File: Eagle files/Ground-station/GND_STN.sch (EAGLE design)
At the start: 43 parts, among them IC1 BMP280, J2 XT60-M, Q3 SI7625DN-T1-GE3, U1 AMS1117-5.0, U2 AMS1117-3.3, U4 SOIC127P790X216-8NW25Q128JVJSQ, X1 USB Type C

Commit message: Added the GND_STN.brd file
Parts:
- removed C10, C11, C12, C15, C16, C4, C5, C8, C9: 100nF, rcl:C-EUC0603
- added R10, R8: 10k, rcl:R-EU_R0603
- added R3, R6: 27.4, rcl:R-EU_R0603
- C13, C18, C2, C3: device rcl:C-EUC0805 -> rcl:C-EUC0603
- C6, C7: value 1uF -> 10uF
- R19, R22, R23, R9: device rcl:R-EU_R0805 -> rcl:R-EU_R0603
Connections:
- removed net 3V3_OP: C10.1, C11.1, C12.1, C15.1, C16.1, C7.1, C8.1, C9.1, RP2040.ADC_AVDD, RP2040.IOVDD0, RP2040.IOVDD1, RP2040.IOVDD2, RP2040.IOVDD3, RP2040.IOVDD4, RP2040.IOVDD5, RP2040.RUN, RP2040.USB_VDD, RP2040.VREG_IN, U4.VCC
- removed net N$3: C2.1
- new net N$4: R3.1, RP2040.USB_DP
- new net N$5: R6.1, RP2040.USB_DM
- new net N$6: C24.2, R1.1, U$3.TRI
- net 1V1: no longer C4.1, C5.1
- net 3V3: now also C7.1, R10.1, R8.2, RP2040.ADC_AVDD, RP2040.IOVDD0, RP2040.IOVDD1, RP2040.IOVDD2, RP2040.IOVDD3, RP2040.IOVDD4, RP2040.IOVDD5, RP2040.RUN, RP2040.USB_VDD, RP2040.VREG_IN, U4.VCC
- net 5V: now also C2.1
- net 5V_BATT: now also D4.A; no longer D4.C, Q3.S_1, Q3.S_2, Q3.S_3
- net D+: now also R3.2
- net D-: now also R6.2
- net GND: no longer C10.2, C11.2, C12.2, C15.2, C16.2, C4.2, C5.2, C8.2, C9.2
- net N$1: now also D4.C, Q3.S_1, Q3.S_2, Q3.S_3; no longer D4.A
- net RSSI: now also RP2040.GPIO23
- net SCK: no longer RP2040.GPIO10
- net TEL_RST: now also RP2040.GPIO22
- net TEL_RX: now also R8.1, RP2040.GPIO24
- net TEL_TX: now also R10.2, RP2040.GPIO25
- net XOUT: no longer C24.2, R1.1, U$3.TRI
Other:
- moved on the sheet: C6

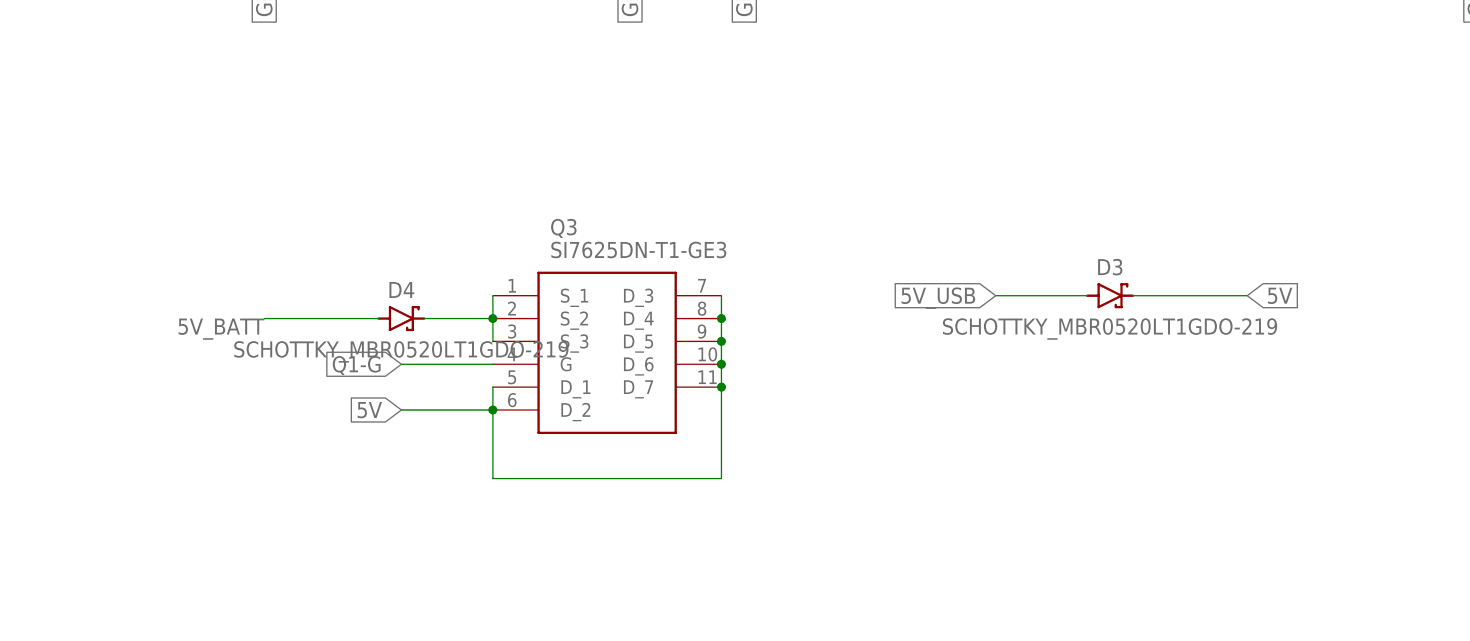
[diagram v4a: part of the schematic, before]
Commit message: Updated the traces
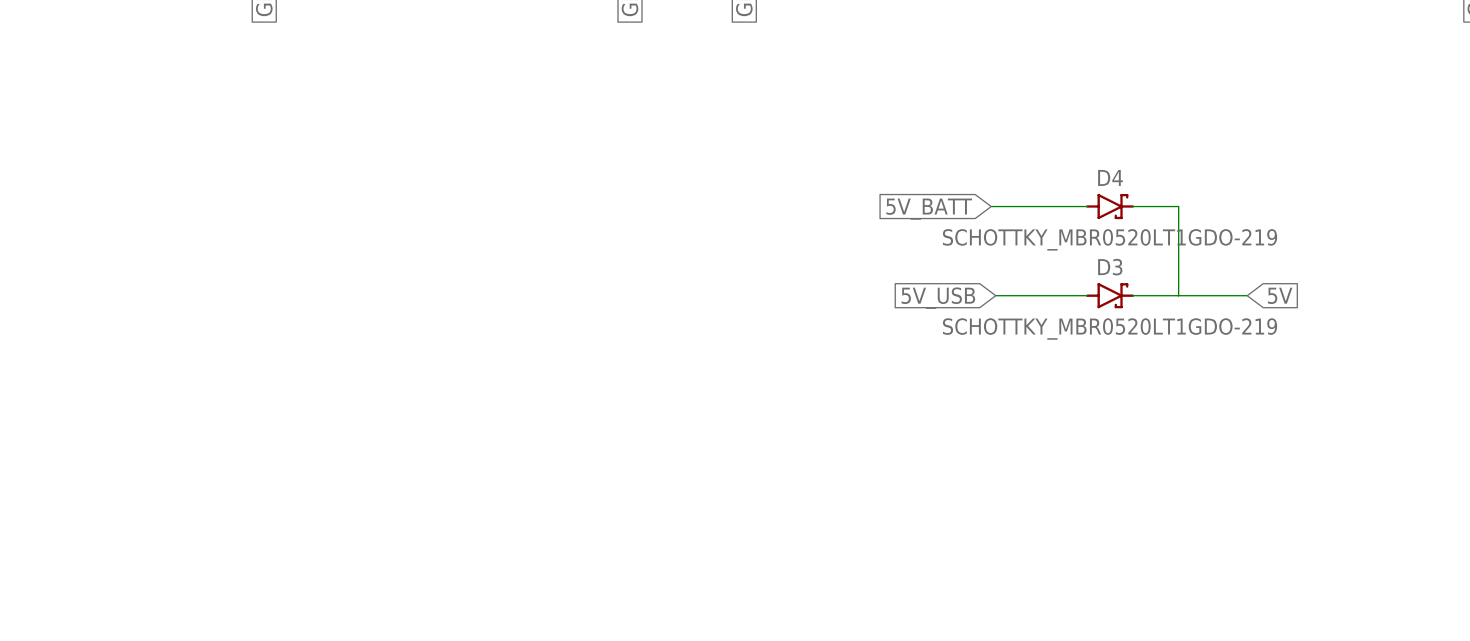
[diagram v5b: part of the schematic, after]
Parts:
- removed Q3: SI7625DN-T1-GE3, SI7625DN-T1-GE3:SI7625DN-T1-GE3
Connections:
- removed net N$1: D4.C, Q3.S_1, Q3.S_2, Q3.S_3
- removed net Q1-G: Q3.G
- net 5V: now also D4.C; no longer Q3.D_1, Q3.D_2, Q3.D_3, Q3.D_4, Q3.D_5, Q3.D_6, Q3.D_7
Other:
- moved on the sheet: D4
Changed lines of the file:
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@@
 <part name="X1" library="microbuilder" deviceset="USB_C" device="" value="USB Type C"/>
 <part name="SV1" library="con-lsta" library_urn="urn:adsk.eagle:library:161" deviceset="FE10-1" device="" package3d_urn="urn:adsk.eagle:package:8192/1"/>
-<part name="Q3" library="SI7625DN-T1-GE3" deviceset="SI7625DN-T1-GE3" device=""/>
 <part name="D3" library="Diode" library_urn="urn:adsk.eagle:library:16378169" deviceset="SCHOTTKY_" device="DO-219" package3d_urn="urn:adsk.eagle:package:9427153/2" technology="MBR0520LT1G"/>
 <part name="D4" library="Diode" library_urn="urn:adsk.eagle:library:16378169" deviceset="SCHOTTKY_" device="DO-219" package3d_urn="urn:adsk.eagle:package:9427153/2" technology="MBR0520LT1G"/>
@@
 <attribute name="NAME" x="-64.77" y="121.158" size="1.778" layer="95" rot="R180"/>
 </instance>
-<instance part="Q3" gate="G$1" x="-513.08" y="88.9" smashed="yes">
-<attribute name="NAME" x="-506.73" y="96.52" size="1.778" layer="95" align="center-left"/>
-<attribute name="VALUE" x="-506.73" y="93.98" size="1.778" layer="96" align="center-left"/>
-</instance>
 <instance part="D3" gate="G$1" x="-444.5" y="88.9" smashed="yes">
 <attribute name="NAME" x="-444.5" y="92.075" size="1.778" layer="95" align="center"/>
 <attribute name="VALUE" x="-444.5" y="85.471" size="1.778" layer="95" align="center"/>
 </instance>
-<instance part="D4" gate="G$1" x="-523.24" y="86.36" smashed="yes">
-<attribute name="NAME" x="-523.24" y="89.535" size="1.778" layer="95" align="center"/>
-<attribute name="VALUE" x="-523.24" y="82.931" size="1.778" layer="95" align="center"/>
+<instance part="D4" gate="G$1" x="-444.5" y="98.806" smashed="yes">
+<attribute name="NAME" x="-444.5" y="101.981" size="1.778" layer="95" align="center"/>
+<attribute name="VALUE" x="-444.5" y="95.377" size="1.778" layer="95" align="center"/>
 </instance>
 <instance part="U2" gate="G$1" x="-386.08" y="139.7" smashed="yes">
@@
 <segment>
 <pinref part="D3" gate="G$1" pin="C"/>
-<wire x1="-441.96" y1="88.9" x2="-429.26" y2="88.9" width="0.1524" layer="91"/>
+<wire x1="-441.96" y1="88.9" x2="-436.88" y2="88.9" width="0.1524" layer="91"/>
 <label x="-429.26" y="88.9" size="1.778" layer="95" xref="yes"/>
-</segment>
-<segment>
-<pinref part="Q3" gate="G$1" pin="D_3"/>
-<pinref part="Q3" gate="G$1" pin="D_4"/>
-<wire x1="-487.68" y1="88.9" x2="-487.68" y2="86.36" width="0.1524" layer="91"/>
-<pinref part="Q3" gate="G$1" pin="D_5"/>
-<wire x1="-487.68" y1="83.82" x2="-487.68" y2="86.36" width="0.1524" layer="91"/>
-<junction x="-487.68" y="86.36"/>
-<pinref part="Q3" gate="G$1" pin="D_6"/>
-<wire x1="-487.68" y1="83.82" x2="-487.68" y2="81.28" width="0.1524" layer="91"/>
-<junction x="-487.68" y="83.82"/>
-<pinref part="Q3" gate="G$1" pin="D_7"/>
-<wire x1="-487.68" y1="81.28" x2="-487.68" y2="78.74" width="0.1524" layer="91"/>
-<junction x="-487.68" y="81.28"/>
-<wire x1="-487.68" y1="78.74" x2="-487.68" y2="68.58" width="0.1524" layer="91"/>
-<junction x="-487.68" y="78.74"/>
-<pinref part="Q3" gate="G$1" pin="D_1"/>
-<pinref part="Q3" gate="G$1" pin="D_2"/>
-<wire x1="-487.68" y1="68.58" x2="-513.08" y2="68.58" width="0.1524" layer="91"/>
-<wire x1="-513.08" y1="78.74" x2="-513.08" y2="76.2" width="0.1524" layer="91"/>
-<wire x1="-513.08" y1="68.58" x2="-513.08" y2="76.2" width="0.1524" layer="91"/>
-<junction x="-513.08" y="76.2"/>
-<wire x1="-513.08" y1="76.2" x2="-523.24" y2="76.2" width="0.1524" layer="91"/>
-<label x="-523.24" y="76.2" size="1.778" layer="95" rot="R180" xref="yes"/>
+<wire x1="-436.88" y1="88.9" x2="-429.26" y2="88.9" width="0.1524" layer="91"/>
+<wire x1="-436.88" y1="88.9" x2="-436.88" y2="98.806" width="0.1524" layer="91"/>
+<pinref part="D4" gate="G$1" pin="C"/>
+<wire x1="-436.88" y1="98.806" x2="-441.96" y2="98.806" width="0.1524" layer="91"/>
 </segment>
 <segment>
@@
 <segment>
 <pinref part="D4" gate="G$1" pin="A"/>
-<wire x1="-525.78" y1="86.36" x2="-538.48" y2="86.36" width="0.1524" layer="91"/>
-<label x="-538.48" y="86.36" size="1.778" layer="95" rot="R180"/>
+<wire x1="-447.04" y1="98.806" x2="-457.708" y2="98.806" width="0.1524" layer="91"/>
+<label x="-457.708" y="98.806" size="1.778" layer="95" rot="R180" xref="yes"/>
 </segment>
 </net>
@@
 </segment>
 </net>
-<net name="Q1-G" class="0">
-<segment>
-<pinref part="Q3" gate="G$1" pin="G"/>
-<wire x1="-513.08" y1="81.28" x2="-523.24" y2="81.28" width="0.1524" layer="91"/>
-<label x="-523.24" y="81.28" size="1.778" layer="95" rot="R180" xref="yes"/>
-</segment>
-</net>
 <net name="SCK" class="0">
 <segment>
@@
 </segment>
 </net>
-<net name="N$1" class="0">
-<segment>
-<pinref part="D4" gate="G$1" pin="C"/>
-<pinref part="Q3" gate="G$1" pin="S_2"/>
-<wire x1="-520.7" y1="86.36" x2="-513.08" y2="86.36" width="0.1524" layer="91"/>
-<pinref part="Q3" gate="G$1" pin="S_1"/>
-<wire x1="-513.08" y1="88.9" x2="-513.08" y2="86.36" width="0.1524" layer="91"/>
-<junction x="-513.08" y="86.36"/>
-<pinref part="Q3" gate="G$1" pin="S_3"/>
-<wire x1="-513.08" y1="83.82" x2="-513.08" y2="86.36" width="0.1524" layer="91"/>
-</segment>
-</net>
